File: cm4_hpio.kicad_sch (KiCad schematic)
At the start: 22 parts, among them CN10 M2 x 2.5mm, CN14 USB4110-GF-A, CN9 TE 1-2199230-6

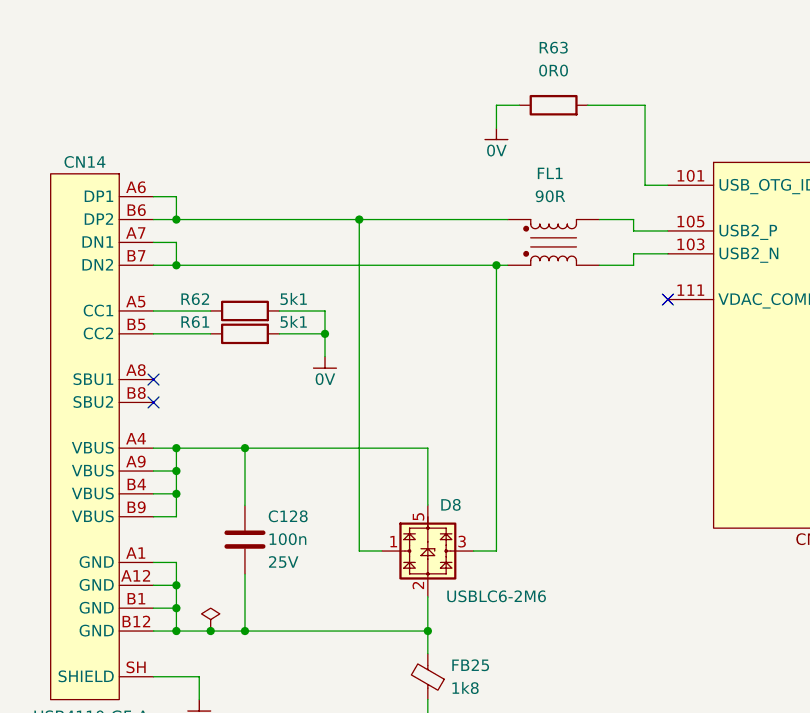
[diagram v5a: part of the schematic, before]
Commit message: Moved to preferred library
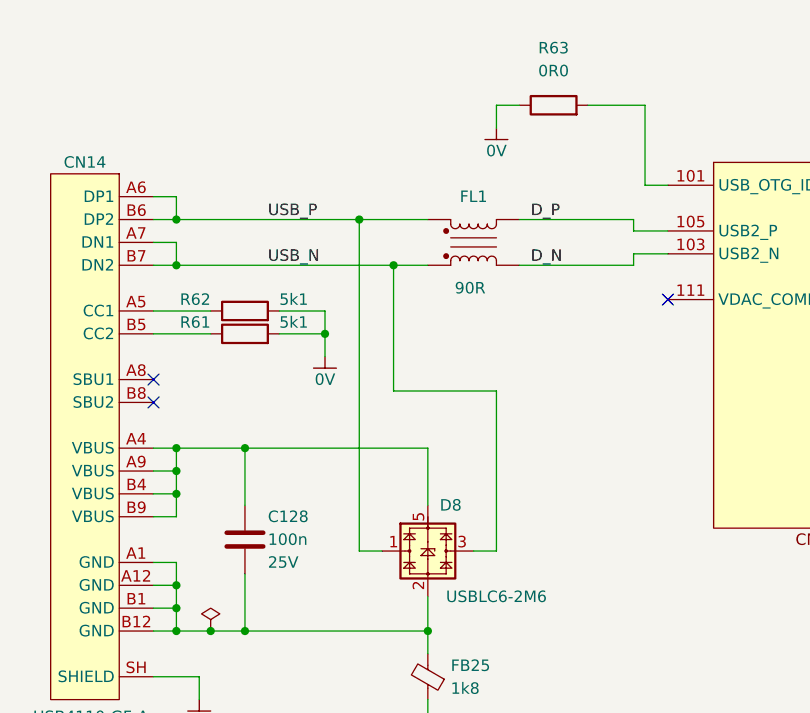
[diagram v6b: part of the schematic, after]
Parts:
- C128: symbol Auto_Library_WUT:Yageo CC0402KRX7R8BB104 -> Preferred_WUT:Yageo CC0402KRX7R8BB104
- D18, D19: symbol Auto_Library_WUT:nexperia PESD3V3U1UB,115 -> Preferred_WUT:nexperia PESD3V3U1UB,115
- FB25: symbol Auto_Library_WUT:Murata BLM15BD182SN1D -> Preferred_WUT:Murata BLM15BD182SN1D
- LD2: symbol Auto_Library_WUT:Ekinglux_E6C0603VGAC1UDA -> Preferred_WUT:Ekinglux_E6C0603VGAC1UDA
- R57: symbol Auto_Library_WUT:KOA Speer RK73H1ETTP1001F -> Preferred_WUT:KOA Speer RK73H1ETTP1001F
- R58, R59: symbol Auto_Library_WUT:KOA Speer RK73H1ETTP1000F -> Preferred_WUT:KOA Speer RK73H1ETTP1000F
- R63: symbol Auto_Library_WUT:KOA Speer RK73Z1ETTP -> Preferred_WUT:KOA Speer RK73Z1ETTP
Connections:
- net USB_P: now reaches CN14.A6 (DP1), CN14.B6 (DP2), D8.1, D8.6
- net USB_P: now also FL1.3; no longer FL1.1
- net USB_N: now reaches CN14.A7 (DN1), CN14.B7 (DN2), D8.3, D8.4
- net USB_N: now also FL1.1; no longer FL1.3
- net D_N: now reaches CN5.103 (USB2_N)
- net D_N: now also FL1.2; no longer FL1.4
- net D_P: now reaches CN5.105 (USB2_P)
- net D_P: now also FL1.4; no longer FL1.2
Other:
- moved on the sheet: FL1
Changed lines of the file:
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@@
   (junction (at 294.64 66.04) (diameter 0) (color 0 0 0 0)
   )
-  (junction (at 83.82 160.02) (diameter 0) (color 0 0 0 0)
-  )
   (junction (at 347.98 48.26) (diameter 0) (color 0 0 0 0)
   )
@@
   (junction (at 289.56 66.04) (diameter 0) (color 0 0 0 0)
   )
+  (junction (at 72.39 160.02) (diameter 0) (color 0 0 0 0)
+  )
   (junction (at 158.75 46.99) (diameter 0) (color 0 0 0 0)
   )
@@
     (stroke (width 0) (type default))
   )
-  (wire (pts (xy 83.82 160.02) (xy 83.82 191.77))
-    (stroke (width 0) (type default))
-  )
   (wire (pts (xy 347.98 99.06) (xy 347.98 96.52))
     (stroke (width 0) (type default))
@@
     (stroke (width 0) (type default))
   )
+  (wire (pts (xy 72.39 160.02) (xy 72.39 173.99))
+    (stroke (width 0) (type default))
+  )
   (wire (pts (xy 246.38 204.47) (xy 243.84 204.47))
     (stroke (width 0) (type default))
@@
     (stroke (width 0) (type default))
   )
-  (wire (pts (xy 48.26 160.02) (xy 83.82 160.02))
-    (stroke (width 0) (type default))
-  )
   (wire (pts (xy 347.98 86.36) (xy 347.98 83.82))
     (stroke (width 0) (type default))
@@
     (stroke (width 0) (type default))
   )
+  (wire (pts (xy 83.82 173.99) (xy 83.82 191.77))
+    (stroke (width 0) (type default))
+  )
   (wire (pts (xy 266.7 66.04) (xy 269.24 66.04))
     (stroke (width 0) (type default))
@@
     (stroke (width 0) (type default))
   )
+  (wire (pts (xy 72.39 173.99) (xy 83.82 173.99))
+    (stroke (width 0) (type default))
+  )
   (wire (pts (xy 292.1 184.15) (xy 294.64 184.15))
     (stroke (width 0) (type default))
@@
     (stroke (width 0) (type default))
   )
-  (wire (pts (xy 68.58 154.94) (xy 85.09 154.94))
+  (wire (pts (xy 68.58 154.94) (xy 76.2 154.94))
     (stroke (width 0) (type default))
   )
@@
     (stroke (width 0) (type default))
   )
+  (wire (pts (xy 72.39 160.02) (xy 76.2 160.02))
+    (stroke (width 0) (type default))
+  )
   (wire (pts (xy 158.75 46.99) (xy 158.75 44.45))
     (stroke (width 0) (type default))
@@
     (stroke (width 0) (type default))
   )
-  (wire (pts (xy 83.82 160.02) (xy 85.09 160.02))
+  (wire (pts (xy 48.26 160.02) (xy 72.39 160.02))
     (stroke (width 0) (type default))
   )
@@
     (stroke (width 0) (type default))
   )
-  (wire (pts (xy 95.25 160.02) (xy 99.06 160.02))
+  (wire (pts (xy 86.36 160.02) (xy 99.06 160.02))
     (stroke (width 0) (type default))
   )
@@
     (stroke (width 0) (type default))
   )
-  (wire (pts (xy 99.06 154.94) (xy 95.25 154.94))
+  (wire (pts (xy 99.06 154.94) (xy 86.36 154.94))
     (stroke (width 0) (type default))
   )
@@
     (effects (font (size 1.27 1.27)) (justify right bottom))
   )
+  (label "USB_N" (at 58.42 160.02 0) (fields_autoplaced)
+    (effects (font (size 1.27 1.27)) (justify left bottom))
+  )
   (label "PCIE_REFCLK_P" (at 223.52 40.64 0) (fields_autoplaced)
     (effects (font (size 1.27 1.27)) (justify left bottom))
   )
+  (label "D_N" (at 87.63 160.02 0) (fields_autoplaced)
+    (effects (font (size 1.27 1.27)) (justify left bottom))
+  )
   (label "PCIE_PER0_P" (at 180.34 166.37 180) (fields_autoplaced)
     (effects (font (size 1.27 1.27)) (justify right bottom))
@@
     (effects (font (size 1.27 1.27)) (justify left bottom))
   )
+  (label "USB_P" (at 58.42 154.94 0) (fields_autoplaced)
+    (effects (font (size 1.27 1.27)) (justify left bottom))
+  )
+  (label "D_P" (at 87.63 154.94 0) (fields_autoplaced)
+    (effects (font (size 1.27 1.27)) (justify left bottom))
+  )
   (label "PCIE_PET0_P" (at 223.52 55.88 0) (fields_autoplaced)
     (effects (font (size 1.27 1.27)) (justify left bottom))
@@
     )
   )
-  (symbol (lib_id "Auto_Library_WUT:nexperia PESD3V3U1UB,115") (at 269.24 119.38 90) (unit 1)
+  (symbol (lib_id "Preferred_WUT:nexperia PESD3V3U1UB,115") (at 269.24 119.38 90) (unit 1)
     (in_bom yes) (on_board yes) (dnp no) (fields_autoplaced)
     (property "Reference" "D18" (at 271.78 117.856 90)
@@
     )
   )
-  (symbol (lib_id "Auto_Library_WUT:KOA Speer RK73Z1ETTP") (at 90.17 142.24 90) (unit 1)
+  (symbol (lib_id "Preferred_WUT:KOA Speer RK73Z1ETTP") (at 90.17 142.24 90) (unit 1)
     (in_bom yes) (on_board yes) (dnp no) (fields_autoplaced)
     (property "Reference" "R63" (at 90.17 135.89 90)
@@
     )
   )
-  (symbol (lib_id "Auto_Library_WUT:KOA Speer RK73H1ETTP1000F") (at 247.65 111.76 90) (unit 1)
+  (symbol (lib_id "Preferred_WUT:KOA Speer RK73H1ETTP1000F") (at 247.65 111.76 90) (unit 1)
     (in_bom yes) (on_board yes) (dnp no)
     (property "Reference" "R59" (at 241.3 110.49 90)
@@
     )
   )
-  (symbol (lib_id "Auto_Library_WUT:Yageo CC0402KRX7R8BB104") (at 55.88 190.5 0) (unit 1)
+  (symbol (lib_id "Preferred_WUT:Yageo CC0402KRX7R8BB104") (at 55.88 190.5 0) (unit 1)
     (in_bom yes) (on_board yes) (dnp no) (fields_autoplaced)
     (property "Reference" "C128" (at 58.42 187.96 0) (do_not_autoplace)
@@
     )
   )
-  (symbol (lib_id "Auto_Library_WUT:Murata BLM15BD182SN1D") (at 76.2 205.74 90) (unit 1)
+  (symbol (lib_id "Preferred_WUT:Murata BLM15BD182SN1D") (at 76.2 205.74 90) (unit 1)
     (in_bom yes) (on_board yes) (dnp no) (fields_autoplaced)
     (property "Reference" "FB25" (at 78.74 204.5081 90)
@@
     )
   )
-  (symbol (lib_id "Auto_Library_WUT:KOA Speer RK73H1ETTP1001F") (at 306.07 119.38 90) (unit 1)
+  (symbol (lib_id "Preferred_WUT:KOA Speer RK73H1ETTP1001F") (at 306.07 119.38 90) (unit 1)
     (in_bom yes) (on_board yes) (dnp no)
     (property "Reference" "R57" (at 306.07 116.84 90)
@@
     )
   )
-  (symbol (lib_id "Auto_Library_WUT:Ekinglux_E6C0603VGAC1UDA") (at 290.83 119.38 0) (unit 1)
+  (symbol (lib_id "Preferred_WUT:Ekinglux_E6C0603VGAC1UDA") (at 290.83 119.38 0) (unit 1)
     (in_bom yes) (on_board yes) (dnp no)
     (property "Reference" "LD2" (at 290.83 116.205 0)
@@
     )
   )
-  (symbol (lib_id "Auto_Library_WUT:Wurth Elektronik 744231091") (at 90.17 157.48 0) (unit 1)
-    (in_bom yes) (on_board yes) (dnp no) (fields_autoplaced)
-    (property "Reference" "FL1" (at 89.789 149.86 0)
+  (symbol (lib_id "Auto_Library_WUT:Wurth Elektronik 744231091") (at 81.28 157.48 0) (mirror x) (unit 1)
+    (in_bom yes) (on_board yes) (dnp no)
+    (property "Reference" "FL1" (at 81.28 152.4 0)
       (effects (font (size 1.27 1.27)))
     )
-    (property "Value" "90R" (at 89.789 152.4 0)
+    (property "Value" "90R" (at 80.899 162.56 0)
       (effects (font (size 1.27 1.27)))
     )
-    (property "Footprint" "Inductor_WUT:L_CommonMode_Wurth_WE-CNSW_0805" (at 88.392 157.48 90)
+    (property "Footprint" "Inductor_WUT:L_CommonMode_Wurth_WE-CNSW_0805" (at 79.502 157.48 90)
       (effects (font (size 1.27 1.27)) hide)
     )
-    (property "Datasheet" "https://www.we-online.com/components/products/datasheet/744231091.pdf" (at 90.17 157.48 0)
+    (property "Datasheet" "https://www.we-online.com/components/products/datasheet/744231091.pdf" (at 81.28 157.48 0)
       (effects (font (size 1.27 1.27)) hide)
     )
-    (property "MPN" "744231091" (at 90.17 157.48 0)
+    (property "MPN" "744231091" (at 81.28 157.48 0)
       (effects (font (size 1.27 1.27)) hide)
     )
-    (property "Manufacturer" "Wurth Elektronik" (at 90.17 157.48 0)
+    (property "Manufacturer" "Wurth Elektronik" (at 81.28 157.48 0)
       (effects (font (size 1.27 1.27)) hide)
     )
-    (property "Height" "1.2mm" (at 90.17 157.48 0)
+    (property "Height" "1.2mm" (at 81.28 157.48 0)
       (effects (font (size 1.27 1.27)) hide)
     )
-    (property "Rated Current" "370mA" (at 90.17 157.48 0)
+    (property "Rated Current" "370mA" (at 81.28 157.48 0)
       (effects (font (size 1.27 1.27)) hide)
     )
@@
     )
   )
-  (symbol (lib_id "Auto_Library_WUT:KOA Speer RK73H1ETTP1000F") (at 157.48 179.07 90) (unit 1)
+  (symbol (lib_id "Preferred_WUT:KOA Speer RK73H1ETTP1000F") (at 157.48 179.07 90) (unit 1)
     (in_bom yes) (on_board yes) (dnp no)
     (property "Reference" "R58" (at 157.48 176.53 90)
@@
     )
   )
-  (symbol (lib_id "Auto_Library_WUT:nexperia PESD3V3U1UB,115") (at 259.08 119.38 90) (unit 1)
+  (symbol (lib_id "Preferred_WUT:nexperia PESD3V3U1UB,115") (at 259.08 119.38 90) (unit 1)
     (in_bom yes) (on_board yes) (dnp no) (fields_autoplaced)
     (property "Reference" "D19" (at 261.62 117.856 90)

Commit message: Started placement
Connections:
- net PCIE_PER0_N: now also D3.1, D3.10 (NC); no longer D3.2, D3.9 (NC)
- net PCIE_PER0_P: now also D3.2, D3.9 (NC); no longer D3.1, D3.10 (NC)
- net PCIE_PET0_N: now also D3.4, D3.7 (NC); no longer D3.5, D3.6 (NC)
- net PCIE_PET0_P: now also D3.5, D3.6 (NC); no longer D3.4, D3.7 (NC)
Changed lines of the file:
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@@
   (junction (at 294.64 181.61) (diameter 0) (color 0 0 0 0)
   )
+  (junction (at 304.8 55.88) (diameter 0) (color 0 0 0 0)
+  )
   (junction (at 294.64 212.09) (diameter 0) (color 0 0 0 0)
   )
@@
   (junction (at 294.64 186.69) (diameter 0) (color 0 0 0 0)
   )
+  (junction (at 304.8 66.04) (diameter 0) (color 0 0 0 0)
+  )
+  (junction (at 294.64 66.04) (diameter 0) (color 0 0 0 0)
+  )
   (junction (at 347.98 86.36) (diameter 0) (color 0 0 0 0)
   )
@@
   (junction (at 209.55 39.37) (diameter 0) (color 0 0 0 0)
   )
+  (junction (at 289.56 66.04) (diameter 0) (color 0 0 0 0)
+  )
   (junction (at 209.55 59.69) (diameter 0) (color 0 0 0 0)
   )
@@
   (junction (at 243.84 212.09) (diameter 0) (color 0 0 0 0)
   )
+  (junction (at 48.26 180.34) (diameter 0) (color 0 0 0 0)
+  )
+  (junction (at 48.26 182.88) (diameter 0) (color 0 0 0 0)
+  )
+  (junction (at 243.84 191.77) (diameter 0) (color 0 0 0 0)
+  )
+  (junction (at 209.55 31.75) (diameter 0) (color 0 0 0 0)
+  )
+  (junction (at 369.57 35.56) (diameter 0) (color 0 0 0 0)
+  )
+  (junction (at 243.84 194.31) (diameter 0) (color 0 0 0 0)
+  )
+  (junction (at 158.75 31.75) (diameter 0) (color 0 0 0 0)
+  )
+  (junction (at 294.64 209.55) (diameter 0) (color 0 0 0 0)
+  )
+  (junction (at 55.88 180.34) (diameter 0) (color 0 0 0 0)
+  )
+  (junction (at 243.84 214.63) (diameter 0) (color 0 0 0 0)
+  )
+  (junction (at 294.64 201.93) (diameter 0) (color 0 0 0 0)
+  )
+  (junction (at 158.75 39.37) (diameter 0) (color 0 0 0 0)
+  )
+  (junction (at 76.2 200.66) (diameter 0) (color 0 0 0 0)
+  )
   (junction (at 299.72 66.04) (diameter 0) (color 0 0 0 0)
   )
-  (junction (at 48.26 180.34) (diameter 0) (color 0 0 0 0)
-  )
-  (junction (at 48.26 182.88) (diameter 0) (color 0 0 0 0)
-  )
-  (junction (at 243.84 191.77) (diameter 0) (color 0 0 0 0)
-  )
-  (junction (at 209.55 31.75) (diameter 0) (color 0 0 0 0)
-  )
-  (junction (at 369.57 35.56) (diameter 0) (color 0 0 0 0)
-  )
-  (junction (at 243.84 194.31) (diameter 0) (color 0 0 0 0)
-  )
-  (junction (at 158.75 31.75) (diameter 0) (color 0 0 0 0)
-  )
-  (junction (at 294.64 209.55) (diameter 0) (color 0 0 0 0)
-  )
-  (junction (at 55.88 180.34) (diameter 0) (color 0 0 0 0)
-  )
-  (junction (at 243.84 214.63) (diameter 0) (color 0 0 0 0)
-  )
-  (junction (at 294.64 201.93) (diameter 0) (color 0 0 0 0)
-  )
-  (junction (at 158.75 39.37) (diameter 0) (color 0 0 0 0)
-  )
-  (junction (at 76.2 200.66) (diameter 0) (color 0 0 0 0)
-  )
   (junction (at 48.26 160.02) (diameter 0) (color 0 0 0 0)
   )
+  (junction (at 289.56 50.8) (diameter 0) (color 0 0 0 0)
+  )
   (junction (at 209.55 62.23) (diameter 0) (color 0 0 0 0)
   )
@@
   (junction (at 347.98 45.72) (diameter 0) (color 0 0 0 0)
   )
-  (junction (at 294.64 66.04) (diameter 0) (color 0 0 0 0)
-  )
   (junction (at 347.98 48.26) (diameter 0) (color 0 0 0 0)
   )
@@
   (junction (at 48.26 198.12) (diameter 0) (color 0 0 0 0)
   )
-  (junction (at 289.56 66.04) (diameter 0) (color 0 0 0 0)
-  )
   (junction (at 72.39 160.02) (diameter 0) (color 0 0 0 0)
   )
@@
   (junction (at 48.26 154.94) (diameter 0) (color 0 0 0 0)
   )
+  (junction (at 299.72 58.42) (diameter 0) (color 0 0 0 0)
+  )
   (junction (at 294.64 194.31) (diameter 0) (color 0 0 0 0)
   )
@@
   (junction (at 243.84 196.85) (diameter 0) (color 0 0 0 0)
   )
+  (junction (at 294.64 48.26) (diameter 0) (color 0 0 0 0)
+  )
   (junction (at 243.84 209.55) (diameter 0) (color 0 0 0 0)
   )
-  (junction (at 299.72 55.88) (diameter 0) (color 0 0 0 0)
-  )
   (junction (at 68.58 154.94) (diameter 0) (color 0 0 0 0)
   )
-  (junction (at 294.64 50.8) (diameter 0) (color 0 0 0 0)
-  )
   (junction (at 64.77 167.64) (diameter 0) (color 0 0 0 0)
   )
-  (junction (at 304.8 66.04) (diameter 0) (color 0 0 0 0)
-  )
-  (junction (at 289.56 48.26) (diameter 0) (color 0 0 0 0)
-  )
   (junction (at 347.98 83.82) (diameter 0) (color 0 0 0 0)
   )
@@
   )
   (junction (at 347.98 68.58) (diameter 0) (color 0 0 0 0)
-  )
-  (junction (at 304.8 58.42) (diameter 0) (color 0 0 0 0)
   )
   (junction (at 347.98 58.42) (diameter 0) (color 0 0 0 0)
@@
     (stroke (width 0) (type default))
   )
-  (wire (pts (xy 223.52 58.42) (xy 304.8 58.42))
-    (stroke (width 0) (type default))
-  )
   (wire (pts (xy 347.98 66.04) (xy 345.44 66.04))
     (stroke (width 0) (type default))
@@
     (stroke (width 0) (type default))
   )
-  (wire (pts (xy 299.72 55.88) (xy 299.72 66.04))
-    (stroke (width 0) (type default))
-  )
-  (wire (pts (xy 223.52 50.8) (xy 294.64 50.8))
-    (stroke (width 0) (type default))
-  )
   (wire (pts (xy 76.2 208.28) (xy 76.2 210.82))
     (stroke (width 0) (type default))
@@
     (stroke (width 0) (type default))
   )
-  (wire (pts (xy 294.64 50.8) (xy 320.04 50.8))
+  (wire (pts (xy 223.52 50.8) (xy 289.56 50.8))
     (stroke (width 0) (type default))
   )
@@
     (stroke (width 0) (type default))
   )
+  (wire (pts (xy 299.72 58.42) (xy 320.04 58.42))
+    (stroke (width 0) (type default))
+  )
   (wire (pts (xy 223.52 40.64) (xy 264.16 40.64))
     (stroke (width 0) (type default))
@@
     (stroke (width 0) (type default))
   )
+  (wire (pts (xy 299.72 58.42) (xy 299.72 66.04))
+    (stroke (width 0) (type default))
+  )
   (wire (pts (xy 243.84 212.09) (xy 243.84 209.55))
     (stroke (width 0) (type default))
@@
     (stroke (width 0) (type default))
   )
+  (wire (pts (xy 289.56 50.8) (xy 320.04 50.8))
+    (stroke (width 0) (type default))
+  )
   (wire (pts (xy 347.98 45.72) (xy 347.98 48.26))
     (stroke (width 0) (type default))
@@
     (stroke (width 0) (type default))
   )
+  (wire (pts (xy 304.8 55.88) (xy 320.04 55.88))
+    (stroke (width 0) (type default))
+  )
   (wire (pts (xy 347.98 86.36) (xy 347.98 83.82))
     (stroke (width 0) (type default))
   )
+  (wire (pts (xy 304.8 55.88) (xy 304.8 66.04))
+    (stroke (width 0) (type default))
+  )
   (wire (pts (xy 64.77 167.64) (xy 64.77 170.18))
     (stroke (width 0) (type default))
@@
     (stroke (width 0) (type default))
   )
+  (wire (pts (xy 294.64 48.26) (xy 294.64 66.04))
+    (stroke (width 0) (type default))
+  )
   (wire (pts (xy 266.7 66.04) (xy 269.24 66.04))
     (stroke (width 0) (type default))
@@
     (stroke (width 0) (type default))
   )
-  (wire (pts (xy 304.8 58.42) (xy 320.04 58.42))
+  (wire (pts (xy 223.52 58.42) (xy 299.72 58.42))
     (stroke (width 0) (type default))
   )
@@
     (stroke (width 0) (type default))
   )
-  (wire (pts (xy 299.72 55.88) (xy 320.04 55.88))
+  (wire (pts (xy 223.52 55.88) (xy 304.8 55.88))
     (stroke (width 0) (type default))
   )
@@
     (stroke (width 0) (type default))
   )
-  (wire (pts (xy 223.52 48.26) (xy 289.56 48.26))
-    (stroke (width 0) (type default))
-  )
   (wire (pts (xy 347.98 53.34) (xy 347.98 55.88))
     (stroke (width 0) (type default))
@@
     (stroke (width 0) (type default))
   )
-  (wire (pts (xy 223.52 55.88) (xy 299.72 55.88))
-    (stroke (width 0) (type default))
-  )
   (wire (pts (xy 243.84 189.23) (xy 243.84 186.69))
     (stroke (width 0) (type default))
@@
     (stroke (width 0) (type default))
   )
-  (wire (pts (xy 294.64 50.8) (xy 294.64 66.04))
-    (stroke (width 0) (type default))
-  )
   (wire (pts (xy 59.69 165.1) (xy 64.77 165.1))
     (stroke (width 0) (type default))
@@
     (stroke (width 0) (type default))
   )
+  (wire (pts (xy 294.64 48.26) (xy 320.04 48.26))
+    (stroke (width 0) (type default))
+  )
   (wire (pts (xy 148.59 179.07) (xy 153.67 179.07))
     (stroke (width 0) (type default))
@@
     (stroke (width 0) (type default))
   )
+  (wire (pts (xy 289.56 50.8) (xy 289.56 66.04))
+    (stroke (width 0) (type default))
+  )
   (wire (pts (xy 68.58 154.94) (xy 76.2 154.94))
     (stroke (width 0) (type default))
@@
     (stroke (width 0) (type default))
   )
-  (wire (pts (xy 304.8 58.42) (xy 304.8 66.04))
-    (stroke (width 0) (type default))
-  )
   (wire (pts (xy 158.75 44.45) (xy 158.75 39.37))
     (stroke (width 0) (type default))
@@
     (stroke (width 0) (type default))
   )
-  (wire (pts (xy 289.56 48.26) (xy 289.56 66.04))
-    (stroke (width 0) (type default))
-  )
   (wire (pts (xy 243.84 214.63) (xy 243.84 212.09))
     (stroke (width 0) (type default))
@@
     (stroke (width 0) (type default))
   )
-  (wire (pts (xy 289.56 48.26) (xy 320.04 48.26))
-    (stroke (width 0) (type default))
-  )
+  (wire (pts (xy 223.52 48.26) (xy 294.64 48.26))
+    (stroke (width 0) (type default))
+  )

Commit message: layout progress
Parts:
- C8: renamed from C128; symbol Preferred_WUT:Yageo CC0402KRX7R8BB104 -> AAA_Preferred_WUT:Yageo CC0402KRX7R8BB104
- D15: renamed from D19; symbol Preferred_WUT:nexperia PESD3V3U1UB,115 -> AAA_Preferred_WUT:nexperia PESD3V3U1UB,115
- D16: renamed from D18; symbol Preferred_WUT:nexperia PESD3V3U1UB,115 -> AAA_Preferred_WUT:nexperia PESD3V3U1UB,115
- FB1: renamed from FB25; symbol Preferred_WUT:Murata BLM15BD182SN1D -> AAA_Preferred_WUT:Murata BLM15BD182SN1D
- LD4: renamed from LD2; symbol Preferred_WUT:Ekinglux_E6C0603VGAC1UDA -> AAA_Preferred_WUT:Ekinglux_E6C0603VGAC1UDA
- R33: renamed from R63; symbol Preferred_WUT:KOA Speer RK73Z1ETTP -> AAA_Preferred_WUT:KOA Speer RK73Z1ETTP
- R34: renamed from R58; symbol Preferred_WUT:KOA Speer RK73H1ETTP1000F -> AAA_Preferred_WUT:KOA Speer RK73H1ETTP1000F
- R35: renamed from R59; symbol Preferred_WUT:KOA Speer RK73H1ETTP1000F -> AAA_Preferred_WUT:KOA Speer RK73H1ETTP1000F
- R36: renamed from R57; symbol Preferred_WUT:KOA Speer RK73H1ETTP1001F -> AAA_Preferred_WUT:KOA Speer RK73H1ETTP1001F
- renumbered C124 to C10, C123 to C9, CN14 to CN5, CN5 to CN6, CN9 to CN7, CN10 to CN8, D8 to D13, D4 to D14, D3 to D17, R62 to R31, R61 to R32
